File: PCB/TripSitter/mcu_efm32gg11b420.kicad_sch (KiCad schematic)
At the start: 22 parts, among them J102 EFM32_PinHeader_PortE, J3 Conn_ARM_JTAG_SWD_20, SW1 SW_Push_Open, U3 IS62WVS2568FBLL-20NLI, U4 EFM32GG11B420F2048GQ100, Y101 48MHz

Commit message: pcb: re-structured PCB schematic layout (#17)
Co-authored-by: Sigvart Hovland <sigvart.m@gmail.com>
Co-authored-by: Ida-Sofie Pettersen <idasofie@Ida-Sofies-MacBook-Air.local>
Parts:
- removed C46, C47, C49, C52, C53, C57: 0.1uF, Capacitor_SMD:C_0201_0603Metric_Pad0.64x0.40mm_HandSolder, symbol Device:C_Small
- removed C54: 10uF, Capacitor_SMD:C_0402_1005Metric_Pad0.74x0.62mm_HandSolder, symbol Device:C_Small
- removed C55, C56: 10nF, Capacitor_SMD:C_0402_1005Metric_Pad0.74x0.62mm_HandSolder, symbol Device:C_Small
- removed C59: 1uF, Capacitor_SMD:C_0201_0603Metric_Pad0.64x0.40mm_HandSolder, symbol Device:C_Small
- removed R19: 100k, Resistor_SMD:R_0805_2012Metric_Pad1.20x1.40mm_HandSolder, symbol Device:R_Small
- added C203, C204, C205, C206, C212, C213: 0.1uF, Capacitor_SMD:C_0402_1005Metric_Pad0.74x0.62mm_HandSolder, symbol Device:C_Small
- added C211: 1uF, Capacitor_SMD:C_0201_0603Metric_Pad0.64x0.40mm_HandSolder, symbol Device:C_Small
- added R804: 100K, Resistor_SMD:R_0805_2012Metric_Pad1.20x1.40mm_HandSolder, symbol Device:R
- C202: renamed from C51; footprint Capacitor_SMD:C_0201_0603Metric_Pad0.64x0.40mm_HandSolder -> Capacitor_SMD:C_0402_1005Metric_Pad0.74x0.62mm_HandSolder; Component Name (none) -> CL10B104KA8NNNC; DK_Ref (none) -> https://www.digikey.no/en/products/detail/samsung-electro-m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
- C210: renamed from C48; footprint Capacitor_SMD:C_0201_0603Metric_Pad0.64x0.40mm_HandSolder -> Capacitor_SMD:C_0402_1005Metric_Pad0.74x0.62mm_HandSolder; DK_Ref (none) -> https://www.digikey.no/no/products/detail/samsung-electro-m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; Digikey_ref https://www.digikey.no/no/products/detail/samsung-electro-m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 -> (none)
- J102: footprint Connector_PinHeader_2.54mm:PinHeader_2x06_P2.54mm_Vertical_SMD -> Connector_PinHeader_1.00mm:PinHeader_2x06_P1.00mm_Vertical
- J201: renamed from J3; footprint Connector_PinHeader_1.00mm:PinHeader_2x10_P1.00mm_Vertical -> Connector_PinHeader_1.27mm:PinHeader_2x10_P1.27mm_Vertical_SMD
- SW1: footprint Button_Switch_SMD:SW_DIP_SPSTx01_Slide_6.7x4.1mm_W8.61mm_P2.54mm_LowProfile -> Button_Switch_SMD:SW_Push_SPST_NO_Alps_SKRK
- renumbered C50 to C201, C58 to C214, U4 to U201, U3 to U202
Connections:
- net +3.3VA is gone; now on net GND: U201.41 (AVDD), U201.45 (AVDD)
- net +3.3V: now also C203.1, C204.1, C205.1, C206.1, C212.1, C213.1, R804.1
- net EFM32_RESETN: now also R804.2
- net GND: now also C203.2, C204.2, C205.2, C206.2, C211.2, C212.2, C213.2
- net PE0_UART0_TX: now also J102.6 (Pin_6); no longer J102.1 (Pin_1)
- net PE1_UART0_RX: now also J102.8 (Pin_8); no longer J102.3 (Pin_3)
- net PE2_UART0_CTS: now also J102.10 (Pin_10); no longer J102.5 (Pin_5)
- net PE3_UART0_RTS: now also J102.12 (Pin_12); no longer J102.7 (Pin_7)
- net PE_4: now also J102.11 (Pin_11); no longer J102.9 (Pin_9)
- net PE_5: now also J102.9 (Pin_9); no longer J102.11 (Pin_11)
- net PE_6: now also J102.7 (Pin_7); no longer J102.10 (Pin_10)
- net PE_7: now also J102.5 (Pin_5); no longer J102.12 (Pin_12)
- net at U201.73 (VREGO): now also C211.1
- net EBI_A0: no longer names the net of U201.37 (PB9)
- net EBI_A1: no longer names the net of U201.26 (PA7)
- net EBI_A10 renamed PD6
- net EBI_A11 renamed PD7
- net EBI_A12 renamed PD8
- net EBI_A13: no longer names the net of U201.46 (PD0)
- net EBI_A14: no longer names the net of U201.47 (PD1)
- net EBI_A15: no longer names the net of U201.48 (PD2)
- net EBI_A16: no longer names the net of U201.9 (PB0)
- net EBI_A17: no longer names the net of U201.10 (PB1)
- net EBI_A18: no longer names the net of U201.11 (PB2)
- net EBI_A19 renamed QSPI0_DQ4
- net EBI_A2: no longer names the net of U201.27 (PA8)
- net EBI_A20 renamed QSPI0_DQ5
- net EBI_A21 renamed QSPI0_DQ6
- net EBI_A22 renamed QSPI0_DQ7
- net EBI_A23: no longer names the net of U201.18 (PC0)
- net EBI_A24: no longer names the net of U201.19 (PC1)
- net EBI_A25: no longer names the net of U201.20 (PC2)
- net EBI_A26: no longer names the net of U201.21 (PC3)
- net EBI_A27: no longer names the net of U201.68 (PC8)
- net EBI_A3: no longer names the net of U201.28 (PA9)
- net EBI_A4: no longer names the net of U201.29 (PA10)
- net EBI_A5: no longer names the net of U201.30 (PA11)
- net EBI_A6: no longer names the net of U201.33 (PA12)
- net EBI_A7: no longer names the net of U201.34 (PA13)
- net EBI_A8: no longer names the net of U201.35 (PA14)
- net EBI_A9: no longer names the net of U201.51 (PD5)
- net EBI_AD0 renamed MCU_PE7
- net EBI_AD1 renamed MCU_PE8
- net EBI_AD10: no longer names the net of U201.2 (PA1)
- net EBI_AD11: no longer names the net of U201.3 (PA2)
- net EBI_AD12: no longer names the net of U201.4 (PA3)
- net EBI_AD13: no longer names the net of U201.5 (PA4)
- net EBI_AD14: no longer names the net of U201.6 (PA5)
- net EBI_AD15: no longer names the net of U201.7 (PA6)
- net EBI_AD2 renamed MCU_PE9
- net EBI_AD3: no longer names the net of U201.95 (PE11)
- net EBI_AD4: no longer names the net of U201.96 (PE12)
- net EBI_AD5: no longer names the net of U201.97 (PE13)
- net EBI_AD6: no longer names the net of U201.98 (PE14)
- net EBI_AD7: no longer names the net of U201.99 (PE15)
- net EBI_AD8: no longer names the net of U201.100 (PA15)
- net EBI_AD9: no longer names the net of U201.1 (PA0)
- net EBI_ALE: no longer names the net of U201.71 (PC11)
- net EBI_ARDY: no longer names the net of J201.13 (TDO/SWO), U201.78 (PF2)
- net EBI_BL0 renamed QSPI_SCLK
- net EBI_BL1 renamed QSPI0_CS0
- net EBI_CS0 renamed QSPI0_DQ0
- net EBI_REn renamed QSPI_DQS
- net EBI_WEn renamed QSPI_CS
- net MCU_EXTIO_PC4: no longer names the net of U201.22 (PC4)
- net MCU_EXTIO_PC4: no longer J102.2 (Pin_2)
- net MCU_EXTIO_PC5: no longer names the net of U201.23 (PC5)
- net MCU_EXTIO_PC5: no longer J102.4 (Pin_4)
- net MCU_EXTIO_PC6: no longer names the net of U201.56 (PC7)
- net MCU_EXTIO_PC6: no longer J102.6 (Pin_6)
- net MCU_EXTIO_PC7: no longer names the net of U201.55 (PC6)
- net MCU_EXTIO_PC7: no longer J102.8 (Pin_8)
- net PF10 renamed USB_D+
- net PF11 renamed USB_D-
- no-connect marks 13 -> 59
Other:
- sheet USB3_micro_ab ports: added EFM32GG11_USB_D+, EFM32GG11_USB_D-; removed EFM32GG11_USB_DM, EFM32GG11_USB_DP

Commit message: mcu debug edit
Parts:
- J201: footprint Connector_PinHeader_1.27mm:PinHeader_2x10_P1.27mm_Vertical_SMD -> Connector_PinHeader_2.54mm:PinHeader_2x10_P2.54mm_Vertical_SMD
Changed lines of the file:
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@@
       (effects (font (size 1.27 1.27)) (justify right))
     )
-    (property "Footprint" "Connector_PinHeader_1.27mm:PinHeader_2x10_P1.27mm_Vertical_SMD" (at 361.95 83.82 0)
+    (property "Footprint" "Connector_PinHeader_2.54mm:PinHeader_2x10_P2.54mm_Vertical_SMD" (at 361.95 83.82 0)
       (effects (font (size 1.27 1.27)) (justify left top) hide)
     )

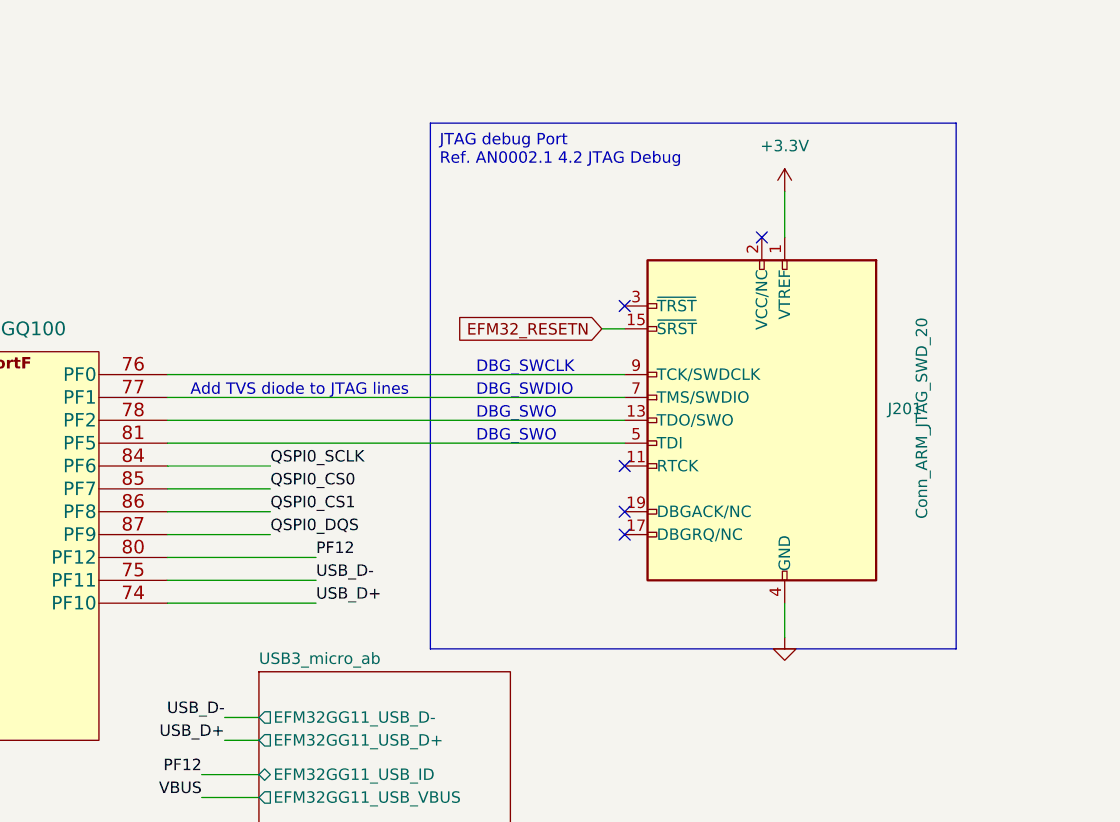
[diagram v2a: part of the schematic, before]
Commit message: edit jtag debug connector
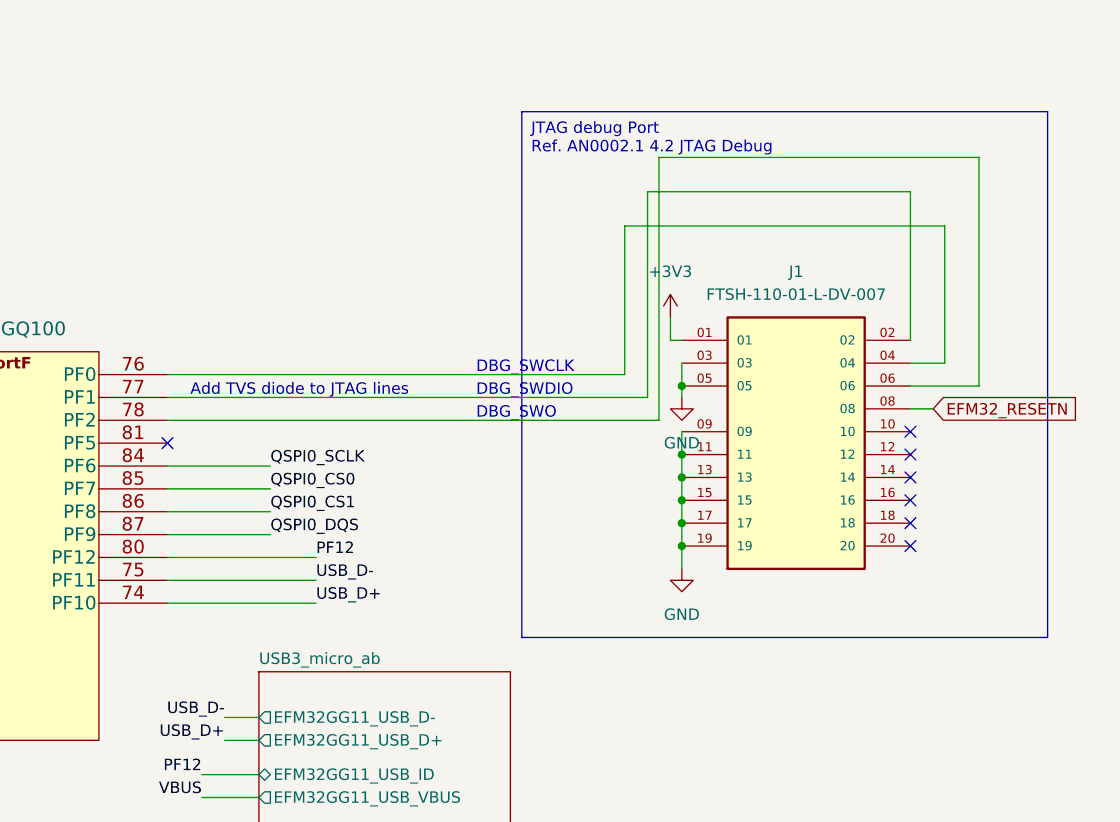
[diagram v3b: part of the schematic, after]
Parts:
- removed J201: Conn_ARM_JTAG_SWD_20, Connector_PinHeader_2.54mm:PinHeader_2x10_P2.54mm_Vertical_SMD, symbol Connector:Conn_ARM_JTAG_SWD_20
- added J1: FTSH-110-01-L-DV-007, FTSH-110-01-L-DV-007:SAMTEC_FTSH-110-01-L-DV-007, symbol FTSH-110-01-L-DV-007:FTSH-110-01-L-DV-007
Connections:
- net EFM32_RESETN: now also J1.08
- net GND: now also J1.03, J1.05, J1.09, J1.11, J1.13, J1.15, J1.17, J1.19
- net at U201.78 (PF2): now also J1.06
- net at U201.77 (PF1): now also J1.02
- net at U201.76 (PF0): now also J1.04
- new net +3V3: J1.01
- no-connect marks 59 -> 61

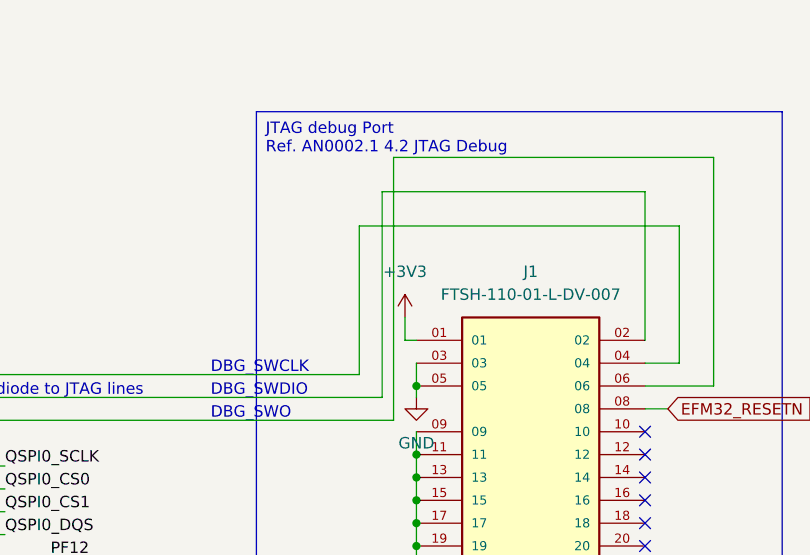
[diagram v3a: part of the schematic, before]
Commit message: fix DRC errors and edit footprint vias
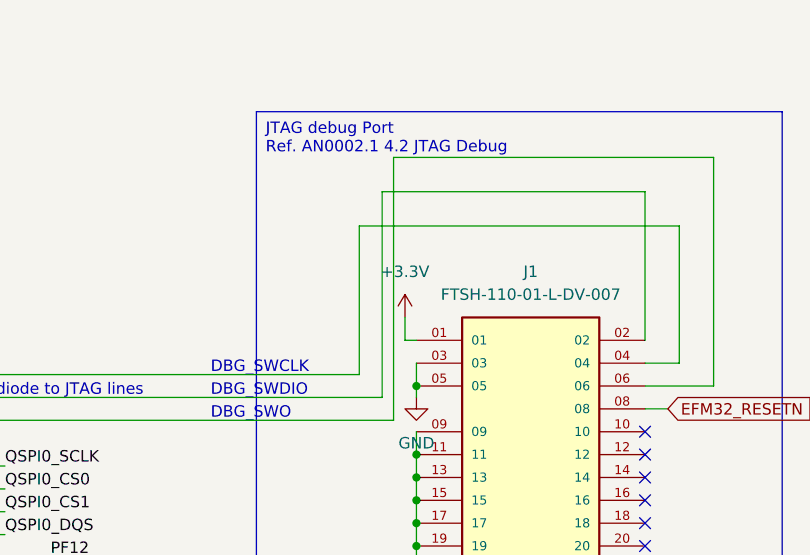
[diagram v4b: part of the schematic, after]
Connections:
- net +3V3 is gone; now on net +3.3V: J1.01
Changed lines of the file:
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@@
-    )
-  )
-  (symbol (lib_id "power:+3V3") (at 363.22 45.72 0) (unit 1)
-    (in_bom yes) (on_board yes) (dnp no) (fields_autoplaced)
-    (property "Reference" "#PWR079" (at 363.22 49.53 0)
-      (effects (font (size 1.27 1.27)) hide)
-    )
-    (property "Value" "+3V3" (at 363.22 40.64 0)
-      (effects (font (size 1.27 1.27)))
-    )
-    (property "Footprint" "" (at 363.22 45.72 0)
-      (effects (font (size 1.27 1.27)) hide)
-    )
-    (property "Datasheet" "" (at 363.22 45.72 0)
-      (effects (font (size 1.27 1.27)) hide)
-    )
-    (pin "1")
-    (instances
-      (project "TripSitter"
-        (path "/5ab65702-9689-4dfd-8f10-6407062323a6/87bcf595-d251-4aa5-8b35-efc055826b19"
-          (reference "#PWR079") (unit 1)
-        )
-      )
     )
   )
@@
         )
       )
+    )
+  )
+  (symbol (lib_id "power:+3.3V") (at 363.22 45.72 0) (unit 1)
+    (in_bom yes) (on_board yes) (dnp no) (fields_autoplaced)
+    (property "Reference" "#PWR071" (at 363.22 49.53 0)
+      (effects (font (size 1.27 1.27)) hide)
+    )
+    (property "Value" "+3.3V" (at 363.22 40.64 0)
+      (effects (font (size 1.27 1.27)))
+    )
+    (property "Footprint" "" (at 363.22 45.72 0)
+      (effects (font (size 1.27 1.27)) hide)
+    )
+    (property "Datasheet" "" (at 363.22 45.72 0)
+      (effects (font (size 1.27 1.27)) hide)
+    )
+    (pin "1")
+    (instances
+      (project "TripSitter"
+        (path "/5ab65702-9689-4dfd-8f10-6407062323a6/87bcf595-d251-4aa5-8b35-efc055826b19"
+          (reference "#PWR071") (unit 1)
+        )
+      )

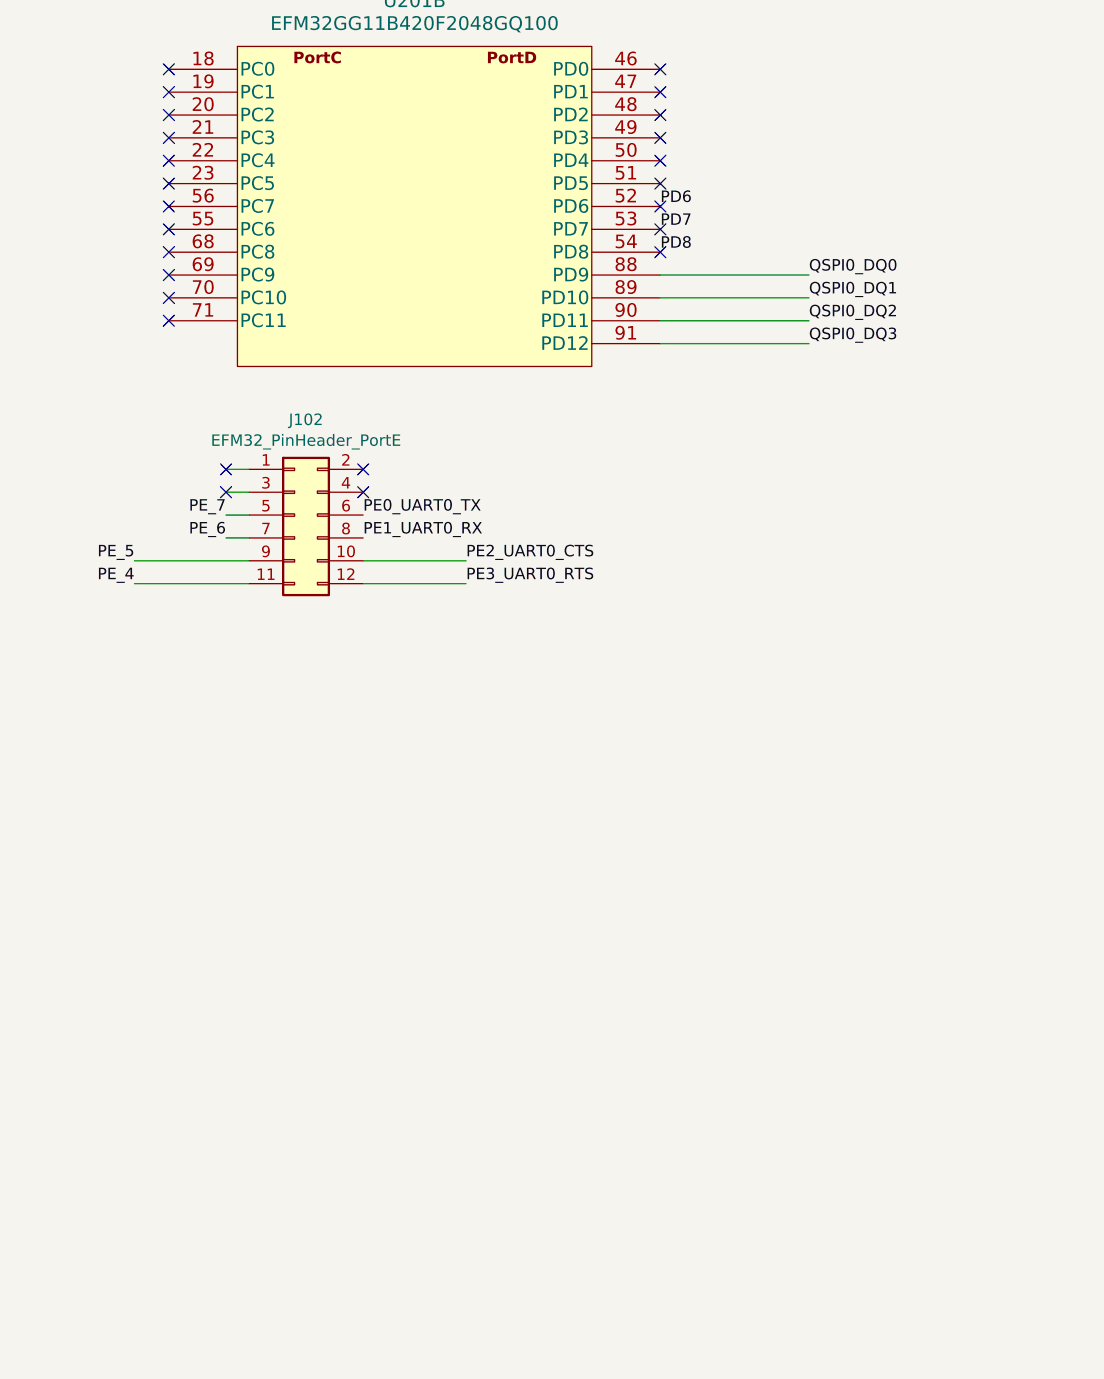
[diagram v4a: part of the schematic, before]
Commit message: pcb: Add buttons
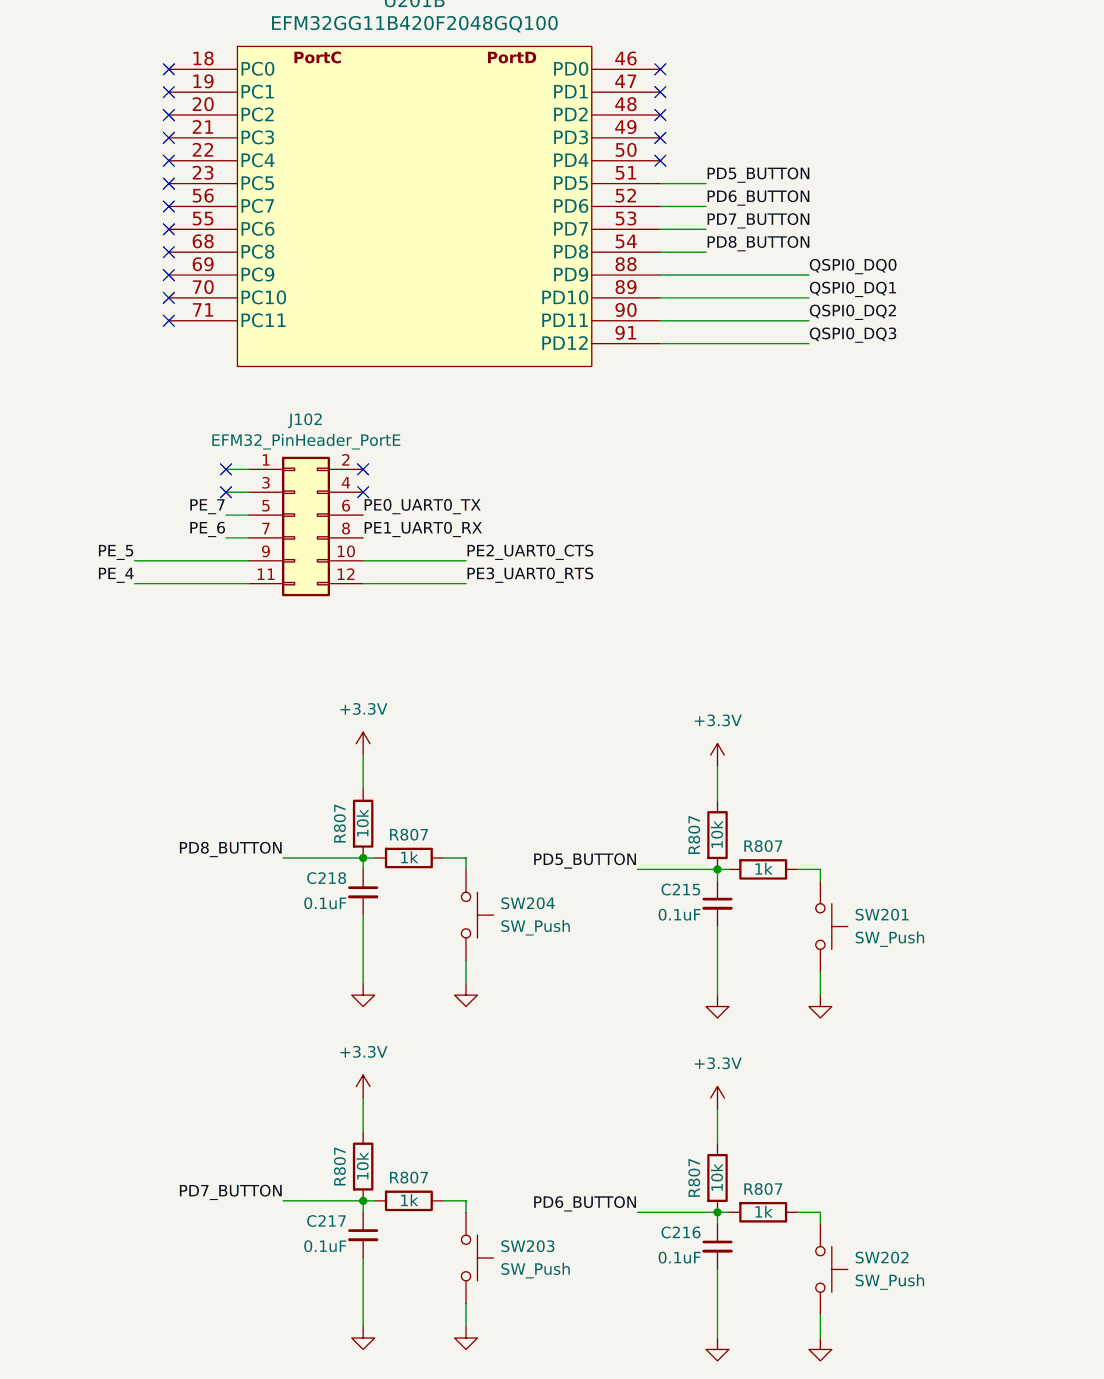
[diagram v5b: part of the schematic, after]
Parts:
- added C215, C216, C217, C218: 0.1uF, Capacitor_SMD:C_0402_1005Metric_Pad0.74x0.62mm_HandSolder, symbol Device:C_Small
- added R807 (x4): 10k, Resistor_SMD:R_0805_2012Metric_Pad1.20x1.40mm_HandSolder, symbol Device:R
- added R807 (x4): 1k, Resistor_SMD:R_0805_2012Metric_Pad1.20x1.40mm_HandSolder, symbol Device:R
- added SW201, SW202, SW203, SW204: SW_Push, Button_Switch_SMD:SW_SPST_Omron_B3FS-100xP, symbol Switch:SW_Push
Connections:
- net +3.3V: now also R807.1, R807.1, R807.1, R807.1
- net GND: now also C215.2, C216.2, C217.2, C218.2, SW201.1, SW202.1, SW203.1, SW204.1
- net PD5_BUTTON: now reaches U201.51 (PD5)
- net PD5_BUTTON: now also C215.1, R807.2, R807.2
- net PD6 renamed PD6_BUTTON
- net PD6_BUTTON: now also C216.1, R807.2, R807.2
- net PD7 renamed PD7_BUTTON
- net PD7_BUTTON: now also C217.1, R807.2, R807.2
- net PD8 renamed PD8_BUTTON
- net PD8_BUTTON: now also C218.1, R807.2, R807.2
- new net: R807.1, SW202.2
- new net: R807.1, SW204.2
- new net: R807.1, SW203.2
- new net: R807.1, SW201.2
- no-connect marks 61 -> 57
